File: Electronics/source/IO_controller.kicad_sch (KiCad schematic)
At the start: 30 parts, among them J10 Conn_01x03, J11 Conn_01x08, J12 Conn_01x08, J13 Conn_01x05, J14 Conn_01x03, J15 Conn_01x06, J8 Conn_01x03, J9 Conn_01x03, U2 TCA9535PWR, U3 TCA9535PWR, U6 MAX11615EEE

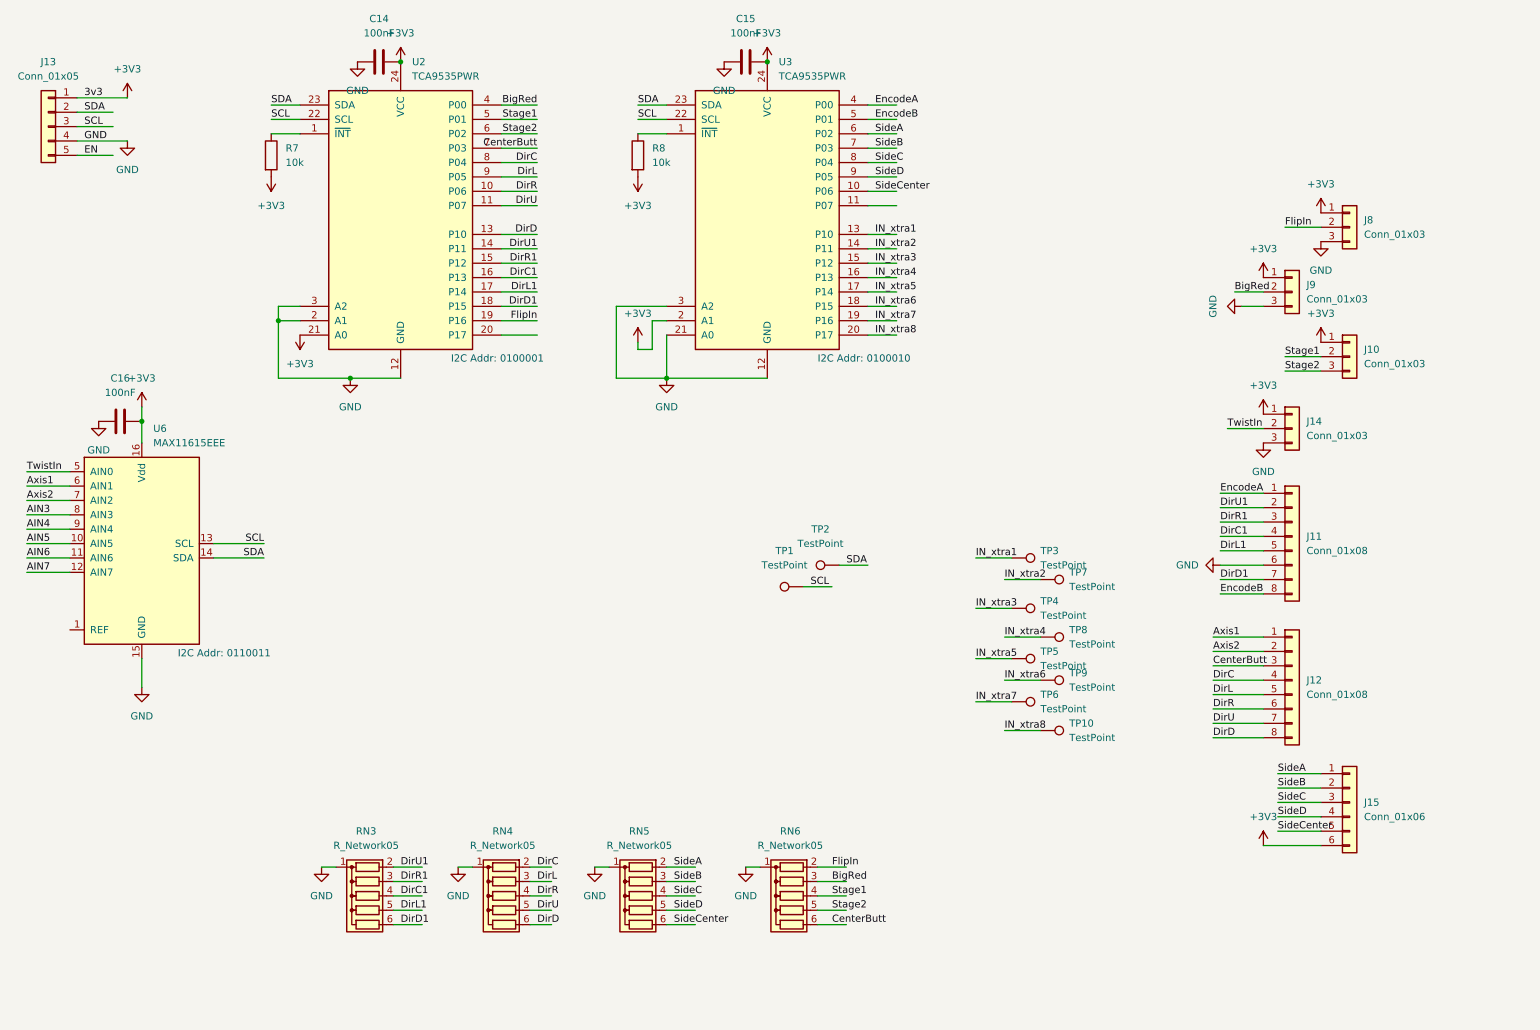
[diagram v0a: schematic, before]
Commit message: Finished first layout of all boards
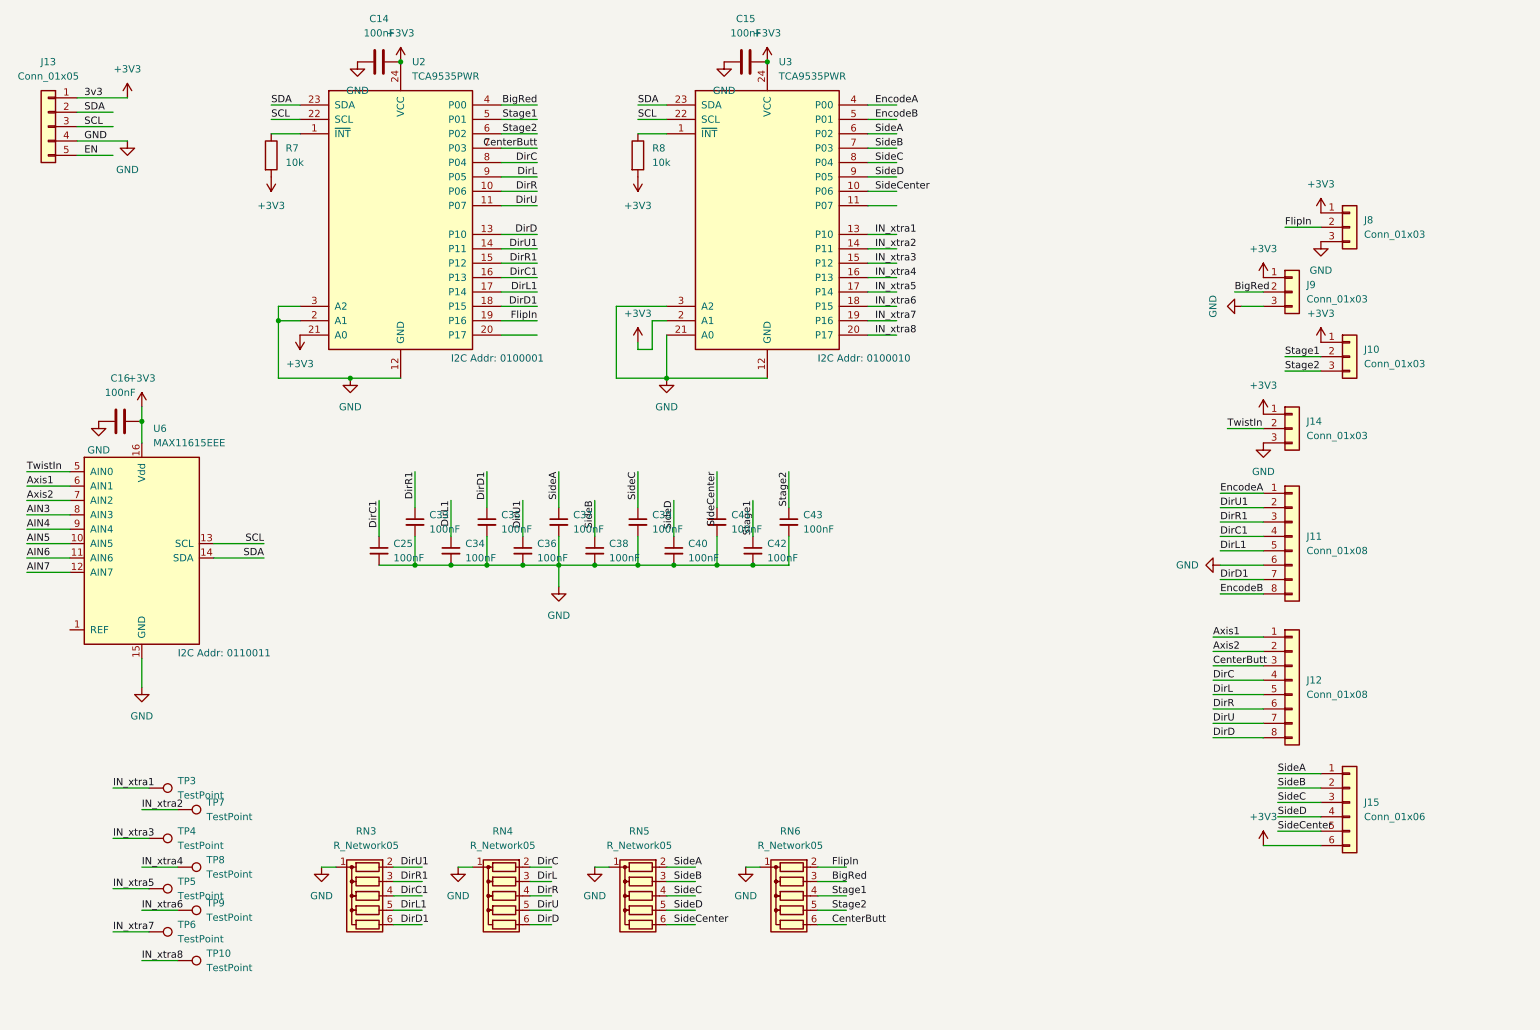
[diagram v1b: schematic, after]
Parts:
- removed TP1, TP2: TestPoint, TestPoint:TestPoint_Pad_D1.0mm, symbol Connector:TestPoint
- added C25, C33, C34, C35, C36, C37, C38, C39, C40, C41, C42, C43: 100nF, Capacitor_SMD:C_0603_1608Metric, symbol Device:C_Small
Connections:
- net DirC1: now also C25.1
- net DirD1: now also C35.1
- net DirL1: now also C34.1
- net DirR1: now also C33.1
- net DirU1: now also C36.1
- net GND: now also C25.2, C33.2, C34.2, C35.2, C36.2, C37.2, C38.2, C39.2, C40.2, C41.2, C42.2, C43.2
- net SideA: now also C37.1
- net SideB: now also C38.1
- net SideC: now also C39.1
- net SideCenter: now also C41.1
- net SideD: now also C40.1
- net Stage1: now also C42.1
- net Stage2: now also C43.1
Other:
- moved on the sheet: TP10, TP3, TP4, TP5, TP6, TP7, TP8, TP9

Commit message: added firmware submodule to firmware repo
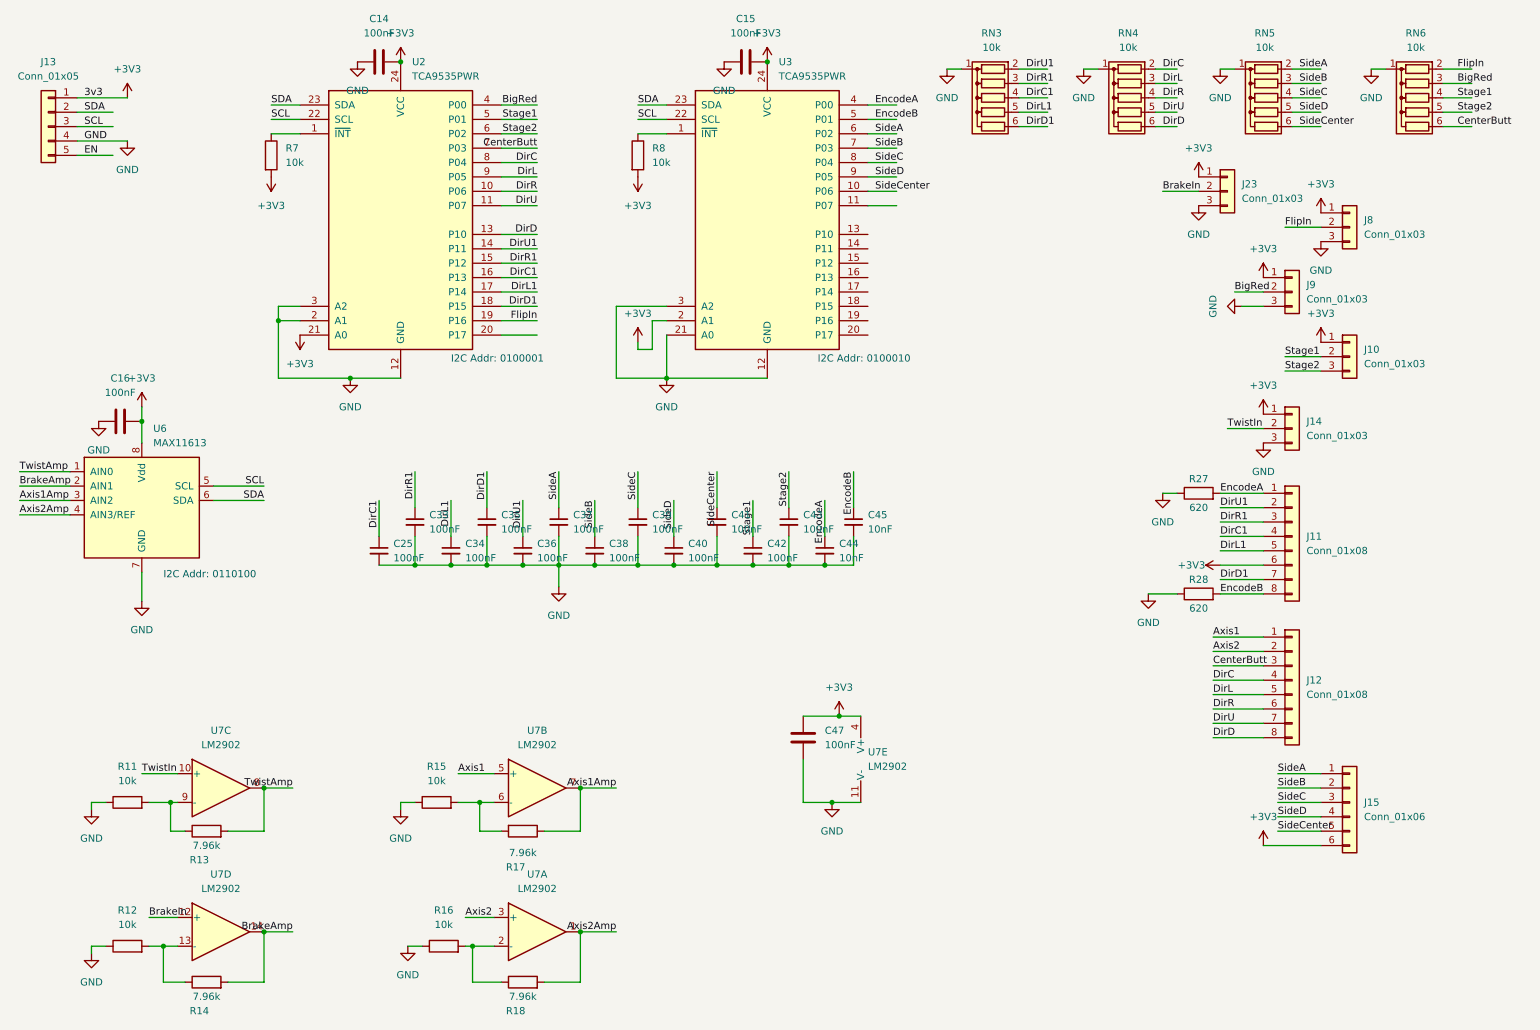
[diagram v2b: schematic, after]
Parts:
- removed TP10, TP3, TP4, TP5, TP6, TP7, TP8, TP9: TestPoint, TestPoint:TestPoint_Pad_D1.0mm, symbol Connector:TestPoint
- removed U6: MAX11615EEE, Package_SO:QSOP-16_3.9x4.9mm_P0.635mm, symbol Analog_ADC:MAX11615
- added C44, C45: 10nF, Capacitor_SMD:C_0603_1608Metric, symbol Device:C_Small
- added C47: 100nF, Capacitor_SMD:C_0603_1608Metric, symbol Device:C
- added J23: Conn_01x03, Connector_JST:JST_PH_B3B-PH-K_1x03_P2.00mm_Vertical, symbol Connector_Generic:Conn_01x03
- added R11, R12, R15, R16: 10k, Resistor_SMD:R_0603_1608Metric, symbol Device:R
- added R13, R14, R17, R18: 7.96k, Resistor_SMD:R_0603_1608Metric, symbol Device:R
- added R27, R28: 620, Resistor_SMD:R_0603_1608Metric, symbol Device:R
- added U6: MAX11613, Package_SO:MSOP-8_3x3mm_P0.65mm, symbol Analog_ADC:MAX11613
- added U7: LM2902, Package_SO:TSSOP-14_4.4x5mm_P0.65mm, symbol Amplifier_Operational:LM2902
- RN3, RN4, RN5, RN6: value R_Network05 -> 10k
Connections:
- net +3V3: now also J11.6 (Pin_6), C47.1, J23.1 (Pin_1), U6.8 (Vdd), U7.4 (V+)
- net Axis1: now also U7.5 (+)
- net Axis2: now also U7.3 (+)
- net EncodeA: now also C44.1, R27.2
- net EncodeB: now also C45.1, R28.2
- net GND: now also C44.2, C45.2, C47.2, J23.3 (Pin_3), R11.1, R12.1, R15.1, R16.1, R27.1, R28.1, U6.7 (GND), U7.11 (V-); no longer J11.6 (Pin_6)
- net SCL: now also U6.5 (SCL)
- net SDA: now also U6.6 (SDA)
- net TwistIn: now also U7.10 (+)
- net IN_xtra1: no longer names the net of U3.13 (P10)
- net IN_xtra2: no longer names the net of U3.14 (P11)
- net IN_xtra3: no longer names the net of U3.15 (P12)
- net IN_xtra4: no longer names the net of U3.16 (P13)
- net IN_xtra5: no longer names the net of U3.17 (P14)
- net IN_xtra6: no longer names the net of U3.18 (P15)
- net IN_xtra7: no longer names the net of U3.19 (P16)
- net IN_xtra8: no longer names the net of U3.20 (P17)
- new net: R12.2, R14.1, U7.13 (-)
- new net: R15.2, R17.2, U7.6 (-)
- new net: R11.2, R13.1, U7.9 (-)
- new net: R16.2, R18.1, U7.2 (-)
- new net Axis1Amp: R17.1, U6.3 (AIN2), U7.7
- new net Axis2Amp: R18.2, U6.4 (AIN3/REF), U7.1
- new net BrakeAmp: R14.2, U6.2 (AIN1), U7.14
- new net BrakeIn: J23.2 (Pin_2), U7.12 (+)
- new net TwistAmp: R13.2, U6.1 (AIN0), U7.8
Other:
- note added: "I2C Addr: 0110100"
- note removed: "I2C Addr: 0110011"
- moved on the sheet: RN3, RN4, RN5, RN6

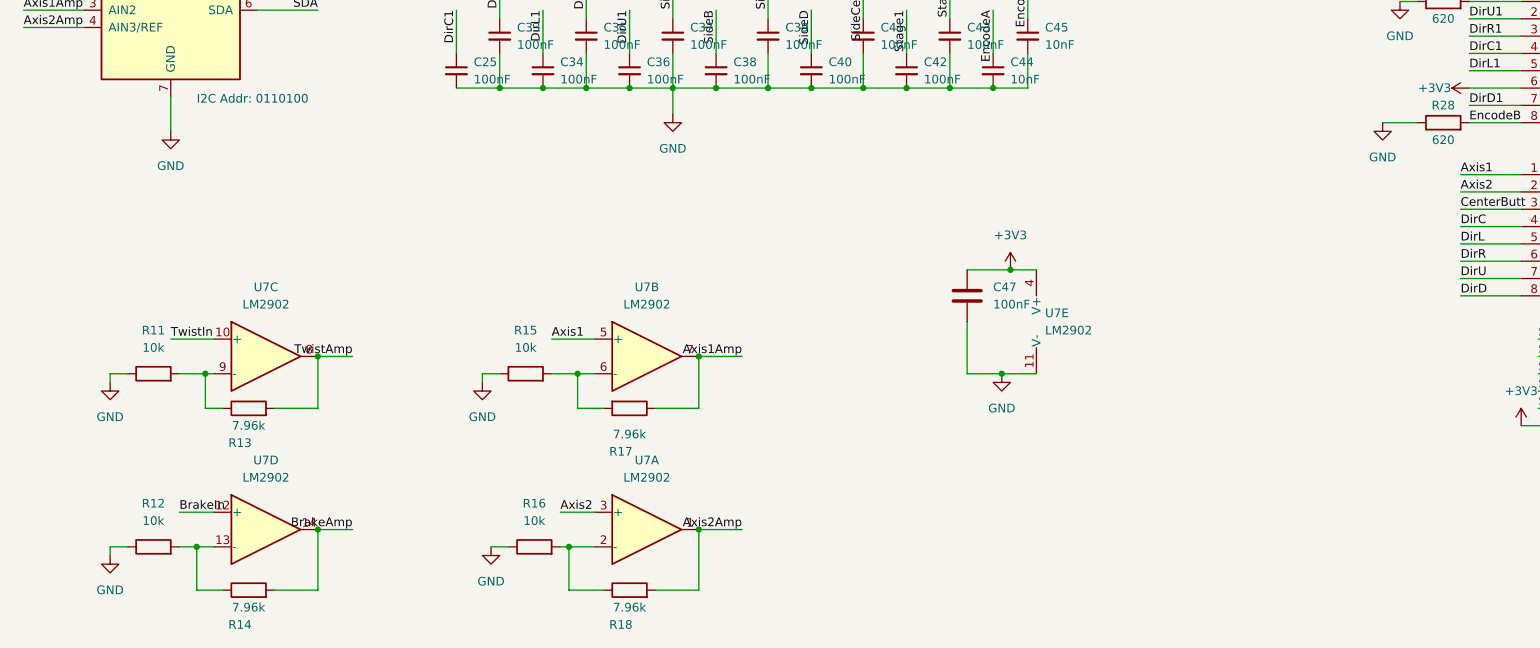
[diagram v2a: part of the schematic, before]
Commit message: implemented MCP6004/9 and rerouted
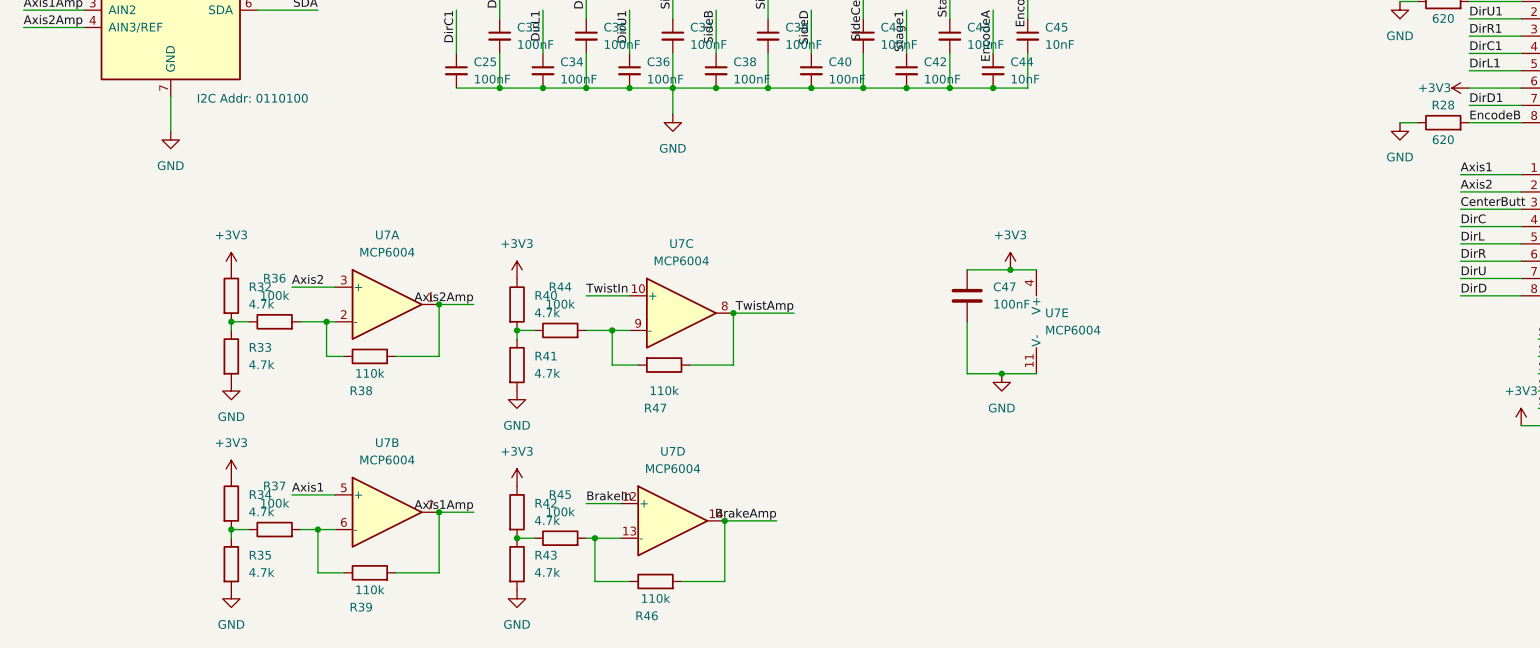
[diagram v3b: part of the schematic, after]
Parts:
- removed R11, R12, R15, R16: 10k, Resistor_SMD:R_0603_1608Metric, symbol Device:R
- removed R13, R14, R17, R18: 7.96k, Resistor_SMD:R_0603_1608Metric, symbol Device:R
- removed U7: LM2902, Package_SO:TSSOP-14_4.4x5mm_P0.65mm, symbol Amplifier_Operational:LM2902
- added R32, R33, R34, R35, R40, R41, R42, R43: 4.7k, Resistor_SMD:R_0603_1608Metric, symbol Device:R
- added R36, R37, R44, R45: 100k, Resistor_SMD:R_0603_1608Metric, symbol Device:R
- added R38, R39, R46, R47: 110k, Resistor_SMD:R_0603_1608Metric, symbol Device:R
- added U7: MCP6004, Package_SO:TSSOP-14_4.4x5mm_P0.65mm, symbol Amplifier_Operational:MCP6004
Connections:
- net +3V3: now also R32.1, R34.1, R40.1, R42.1, U7.4 (V+)
- net Axis1: now also U7.5 (+)
- net Axis1Amp: now also R39.2, U7.7
- net Axis2: now also U7.3 (+)
- net Axis2Amp: now also R38.2, U7.1
- net BrakeAmp: now also R46.2, U7.14
- net BrakeIn: now also U7.12 (+)
- net GND: now also R33.2, R35.2, R41.2, R43.2, U7.11 (V-)
- net TwistAmp: now also R47.1, U7.8
- net TwistIn: now also U7.10 (+)
- new net: R32.2, R33.1, R36.1
- new net: R42.2, R43.1, R45.1
- new net: R45.2, R46.1, U7.13 (-)
- new net: R37.2, R39.1, U7.6 (-)
- new net: R34.2, R35.1, R37.1
- new net: R44.2, R47.2, U7.9 (-)
- new net: R36.2, R38.1, U7.2 (-)
- new net: R40.2, R41.1, R44.1
